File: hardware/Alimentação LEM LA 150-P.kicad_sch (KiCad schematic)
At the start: 8 parts, among them J4 Conn_01x04, J5 Conn_01x04, U2 L7815, U3 L7815

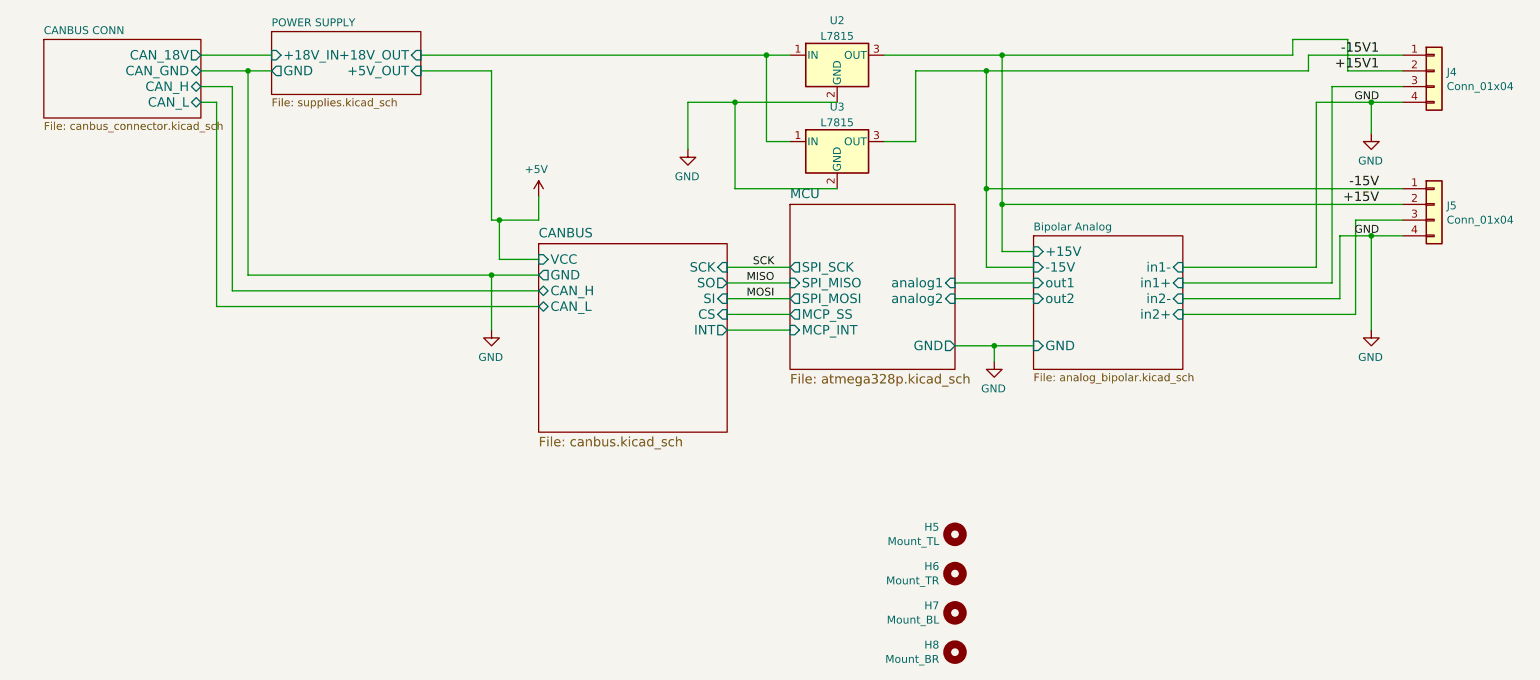
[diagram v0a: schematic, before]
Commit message: Troca do atmega328p -> STM32F103C8T Já que tem CAN integrado e ADC 12 bits (ao invés de 10)
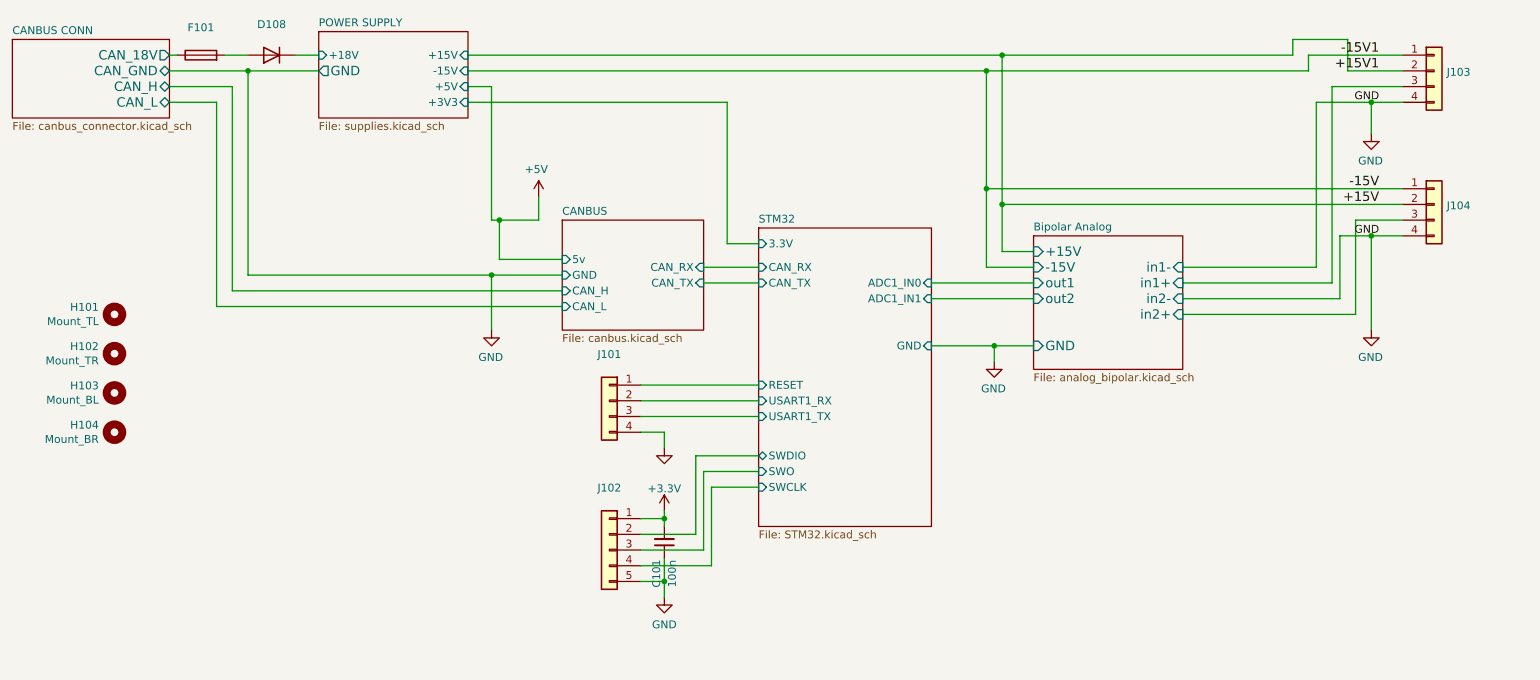
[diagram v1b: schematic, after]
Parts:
- removed U2, U3: L7815, KicadZeniteSolarLibrary18:TO-220-3_Horizontal_Tabless_SMD, symbol Regulator_Linear:L7815
- added C101: 100n, symbol Device:C_Small
- added D108: (no value), symbol Diode:LL4148
- added F101: (no value), symbol Device:Fuse
- added J101: (no value), symbol Connector_Generic:Conn_01x04
- added J102: (no value), symbol Connector_Generic:Conn_01x05
- J103: renamed from J4; value Conn_01x04 -> (none); footprint Connector_Phoenix_MSTB:PhoenixContact_MSTBA_2,5_4-G-5,08_1x04_P5.08mm_Horizontal -> (none)
- J104: renamed from J5; value Conn_01x04 -> (none); footprint Connector_Phoenix_MSTB:PhoenixContact_MSTBA_2,5_4-G-5,08_1x04_P5.08mm_Horizontal -> (none)
- renumbered H5 to H101, H6 to H102, H7 to H103, H8 to H104
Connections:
- net CANBUS CONN/CAN_18V: now also F101.1
- net GND: now also C101.1, J101.4 (Pin_4), J102.5 (Pin_5)
- new net: D108.2 (A), F101.2
- new net +3V3: C101.2, J102.1 (Pin_1)
- new net POWER SUPPLY/+18V: D108.1 (K)
- new net STM32/RESET: J101.1 (Pin_1)
- new net STM32/SWCLK: J102.4 (Pin_4)
- new net STM32/SWDIO: J102.2 (Pin_2)
- new net STM32/SWO: J102.3 (Pin_3)
- new net STM32/USART1_RX: J101.2 (Pin_2)
- new net STM32/USART1_TX: J101.3 (Pin_3)
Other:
- removed sheet MCU
- added sheet STM32 (STM32.kicad_sch)
- sheet CANBUS ports: added 5v, CAN_RX, CAN_TX; removed CS, INT, SCK, SI, SO, VCC
- sheet POWER SUPPLY ports: added +15V, +18V, +3V3, +5V, -15V; removed +18V_IN, +18V_OUT, +5V_OUT
- moved on the sheet: H101, H102, H103, H104

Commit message: Primeiro protótipo da PCB
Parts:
- C101: footprint (none) -> Capacitor_SMD:C_0603_1608Metric_Pad1.08x0.95mm_HandSolder
- D108: value (none) -> LL4148; footprint (none) -> Diode_SMD:D_MiniMELF
- F101: value (none) -> Fuse; footprint (none) -> Fuse:Fuse_1812_4532Metric_Pad1.30x3.40mm_HandSolder
- J101: value (none) -> USART; footprint (none) -> Connector_PinHeader_2.54mm:PinHeader_1x04_P2.54mm_Vertical_SMD_Pin1Left
- J102: value (none) -> STLink; footprint (none) -> Connector_PinHeader_2.54mm:PinHeader_1x05_P2.54mm_Vertical_SMD_Pin1Left
- J103: value (none) -> Sensor1; footprint (none) -> Connector_Phoenix_MSTB:PhoenixContact_MSTBA_2,5_4-G-5,08_1x04_P5.08mm_Horizontal
- J104: value (none) -> Sensor2; footprint (none) -> Connector_Phoenix_MSTB:PhoenixContact_MSTBA_2,5_4-G-5,08_1x04_P5.08mm_Horizontal
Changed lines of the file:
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@@
       (effects (font (size 1.27 1.27)) (justify left))
     )
-    (property "Value" "" (id 1) (at 252.222 71.0946 0)
-      (effects (font (size 1.27 1.27)) (justify left))
-    )
-    (property "Footprint" "" (id 2) (at 250.19 68.58 0)
+    (property "Value" "Sensor1" (id 1) (at 252.222 71.0946 0)
+      (effects (font (size 1.27 1.27)) (justify left))
+    )
+    (property "Footprint" "Connector_Phoenix_MSTB:PhoenixContact_MSTBA_2,5_4-G-5,08_1x04_P5.08mm_Horizontal" (id 2) (at 250.19 68.58 0)
       (effects (font (size 1.27 1.27)) hide)
     )
@@
       (effects (font (size 1.27 1.27)) (justify left))
     )
-    (property "Value" "" (id 1) (at 252.222 92.6846 0)
-      (effects (font (size 1.27 1.27)) (justify left))
-    )
-    (property "Footprint" "" (id 2) (at 250.19 90.17 0)
+    (property "Value" "Sensor2" (id 1) (at 252.222 92.6846 0)
+      (effects (font (size 1.27 1.27)) (justify left))
+    )
+    (property "Footprint" "Connector_Phoenix_MSTB:PhoenixContact_MSTBA_2,5_4-G-5,08_1x04_P5.08mm_Horizontal" (id 2) (at 250.19 90.17 0)
       (effects (font (size 1.27 1.27)) hide)
     )
@@
       (effects (font (size 1.27 1.27)) hide)
     )
-    (property "Value" "" (id 1) (at 125.73 133.9834 0))
+    (property "Value" "GND" (id 1) (at 125.73 133.9834 0))
     (property "Footprint" "" (id 2) (at 125.73 129.54 0)
       (effects (font (size 1.27 1.27)) hide)
@@
     (in_bom yes) (on_board yes) (fields_autoplaced)
     (property "Reference" "D108" (id 0) (at 62.23 61.0702 0))
-    (property "Value" "" (id 1) (at 62.23 63.6071 0))
-    (property "Footprint" "" (id 2) (at 62.23 61.595 0)
+    (property "Value" "LL4148" (id 1) (at 62.23 63.6071 0))
+    (property "Footprint" "Diode_SMD:D_MiniMELF" (id 2) (at 62.23 61.595 0)
       (effects (font (size 1.27 1.27)) hide)
     )
@@
     (in_bom yes) (on_board yes) (fields_autoplaced)
     (property "Reference" "J101" (id 0) (at 116.84 114.4102 0))
-    (property "Value" "" (id 1) (at 116.84 116.9471 0))
-    (property "Footprint" "" (id 2) (at 116.84 121.92 0)
+    (property "Value" "USART" (id 1) (at 116.84 116.9471 0))
+    (property "Footprint" "Connector_PinHeader_2.54mm:PinHeader_1x04_P2.54mm_Vertical_SMD_Pin1Left" (id 2) (at 116.84 121.92 0)
       (effects (font (size 1.27 1.27)) hide)
     )
@@
     (in_bom yes) (on_board yes) (fields_autoplaced)
     (property "Reference" "J102" (id 0) (at 116.84 136.0002 0))
-    (property "Value" "" (id 1) (at 116.84 138.5371 0))
-    (property "Footprint" "" (id 2) (at 116.84 146.05 0)
+    (property "Value" "STLink" (id 1) (at 116.84 138.5371 0))
+    (property "Footprint" "Connector_PinHeader_2.54mm:PinHeader_1x05_P2.54mm_Vertical_SMD_Pin1Left" (id 2) (at 116.84 146.05 0)
       (effects (font (size 1.27 1.27)) hide)
     )
@@
     (in_bom yes) (on_board yes) (fields_autoplaced)
     (property "Reference" "F101" (id 0) (at 50.8 61.5782 90))
-    (property "Value" "" (id 1) (at 50.8 64.1151 90))
-    (property "Footprint" "" (id 2) (at 50.8 67.818 90)
+    (property "Value" "Fuse" (id 1) (at 50.8 64.1151 90))
+    (property "Footprint" "Fuse:Fuse_1812_4532Metric_Pad1.30x3.40mm_HandSolder" (id 2) (at 50.8 67.818 90)
       (effects (font (size 1.27 1.27)) hide)
     )
@@
     (property "Reference" "C101" (id 0) (at 124.46 149.86 90))
     (property "Value" "100n" (id 1) (at 127 149.86 90))
-    (property "Footprint" "" (id 2) (at 125.73 144.78 0)
+    (property "Footprint" "Capacitor_SMD:C_0603_1608Metric_Pad1.08x0.95mm_HandSolder" (id 2) (at 125.73 144.78 0)
       (effects (font (size 1.27 1.27)) hide)
     )
@@
     )
     (path "/ddf05078-8917-4f23-81a6-ce1b6ac52ab3/00000000-0000-0000-0000-00006093192a"
-      (reference "D107") (unit 1) (value "~") (footprint "Package_TO_SOT_SMD:SOT-23")
+      (reference "D107") (unit 1) (value "pesd1can") (footprint "Package_TO_SOT_SMD:SOT-23")
     )
     (path "/7abb686a-cb0e-46e3-9368-9465332545bd"
@@
       (reference "TP112") (unit 1) (value "op_b_out") (footprint "TestPoint:TestPoint_Pad_2.0x2.0mm")
     )
+    (path "/ddf05078-8917-4f23-81a6-ce1b6ac52ab3/5c1c784e-aa61-4b93-a8a6-989fe111598e"
+      (reference "TP501") (unit 1) (value "TxCAN") (footprint "TestPoint:TestPoint_Pad_2.0x2.0mm")
+    )
+    (path "/ddf05078-8917-4f23-81a6-ce1b6ac52ab3/e1ef8bdd-0588-4ddc-96cf-b8b3d064c2c4"
+      (reference "TP502") (unit 1) (value "RxCAN") (footprint "TestPoint:TestPoint_Pad_2.0x2.0mm")
+    )
+    (path "/ddf05078-8917-4f23-81a6-ce1b6ac52ab3/1e58ffc7-8d50-4250-bea4-a79ddbf6a0f0"
+      (reference "TP503") (unit 1) (value "CAN_H") (footprint "TestPoint:TestPoint_Pad_2.0x2.0mm")
+    )
+    (path "/ddf05078-8917-4f23-81a6-ce1b6ac52ab3/52f36df2-cb97-45c3-a7ed-09f3d5c1571b"
+      (reference "TP504") (unit 1) (value "CAN_L") (footprint "TestPoint:TestPoint_Pad_2.0x2.0mm")
+    )
     (path "/00000000-0000-0000-0000-000062102577/00000000-0000-0000-0000-00006222b32c"
